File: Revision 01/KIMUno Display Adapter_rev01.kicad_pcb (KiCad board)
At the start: 2 copper layers, 50.8 x 20.1 mm, 3 parts

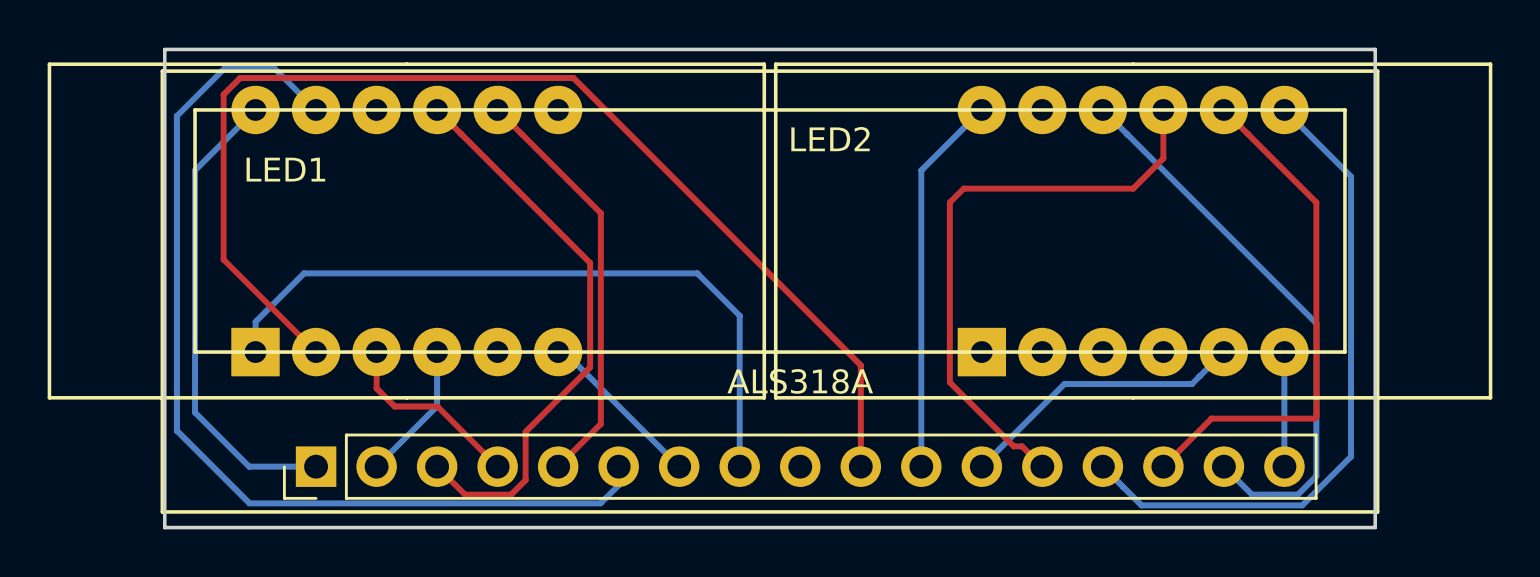
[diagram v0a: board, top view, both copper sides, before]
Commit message: Several changes
Redid the routing.
Changed the LED footprint with smaller pads.
Added logo to underside of the board.
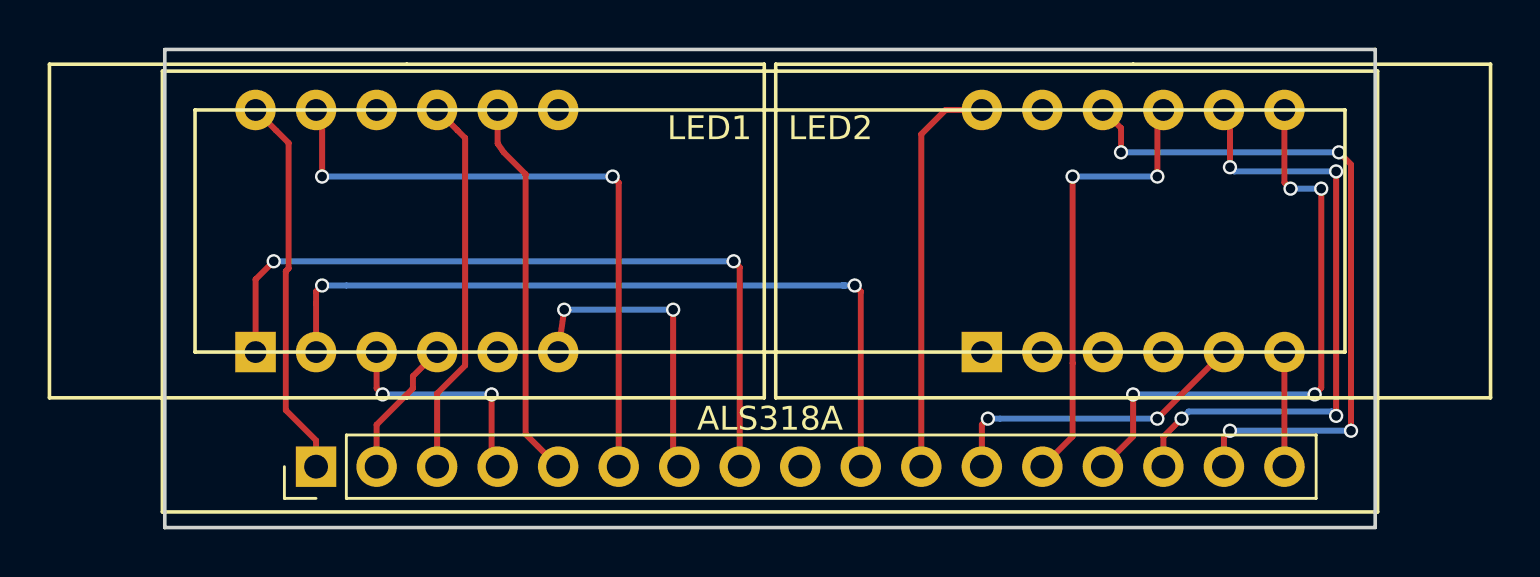
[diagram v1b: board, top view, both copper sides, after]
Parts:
- added  : , Thilo_Lib:LOGO_VintageProject_B.SilkS, F.Cu at (115.8, 69.6)
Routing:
- net /Seg_1d: track 48.7 -> 33.1 mm, vias 0 -> 2
- net /Seg_1a: track 41.5 -> 27.4 mm, vias 0 -> 2
- net /CC2: track 23.8 -> 16.3 mm
- net /CC4: track 7.07 -> 13.3 mm, vias 0 -> 2
- net /Seg_2f: track 23.8 -> 29.8 mm, vias 0 -> 4
- net /CC7: track 24.7 -> 19.2 mm, vias 0 -> 2
- net /CC8: track 21.8 -> 26.3 mm, vias 0 -> 4
- net /CC1: track 19.8 -> 16.1 mm
- net /Seg_2b: track 27.6 -> 24.6 mm, vias 1 -> 4
- net /Seg_1e: track 29.5 -> 32.2 mm, vias 0 -> 2
- net /Seg_1h: track 7.97 -> 9.59 mm, vias 0 -> 2
- net /CC3: track 17.5 -> 16.4 mm
- net /Seg_2g: track 12.2 -> 13.2 mm, vias 0 -> 2
- net /CC6: track 16.0 -> 16.9 mm
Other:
- board text added: "2018"
- board text added: "Rev. 01 / 2018-07-24"
- board text removed: "(c) 2018 VintageProject"
- board text removed: "Rev. 01 / 2018-07-23"

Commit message: Rerouted tracks - Short Board for ALS318A
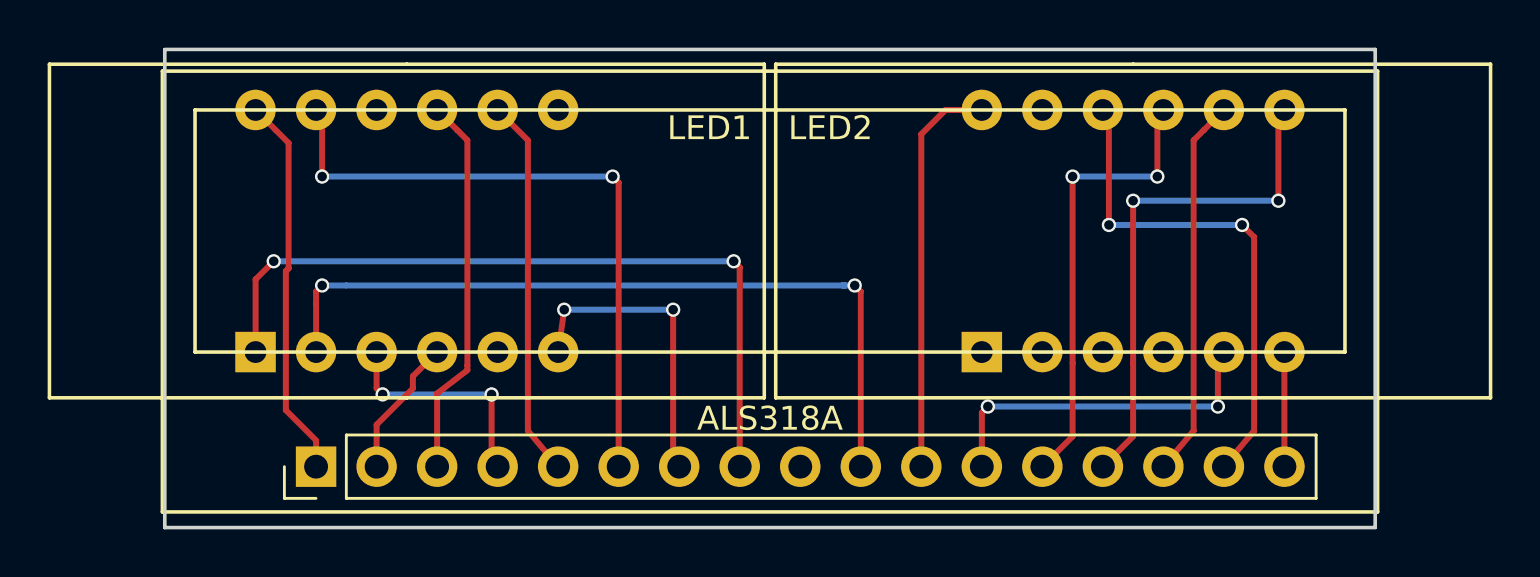
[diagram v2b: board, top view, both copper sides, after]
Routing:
- net /CC8: track 26.3 -> 16.0 mm, vias 4 -> 0
- net /Seg_2f: track 29.8 -> 21.3 mm, vias 4 -> 2
- net /Seg_2b: track 24.6 -> 21.7 mm, vias 4 -> 2
- net /Seg_2g: track 13.2 -> 14.7 mm
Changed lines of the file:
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@@
     (thickness 1.6)
     (drawings 7)
-    (tracks 120)
+    (tracks 100)
     (zones 0)
     (modules 4)
@@
   (segment (start 87.376 62.484) (end 87.63 62.23) (width 0.25) (layer F.Cu) (net 2))
   (segment (start 88.479999 63.079999) (end 87.63 62.23) (width 0.25) (layer F.Cu) (net 2))
-  (segment (start 88.805001 63.405001) (end 88.479999 63.079999) (width 0.25) (layer F.Cu) (net 2))
-  (segment (start 88.805001 72.954001) (end 88.805001 63.405001) (width 0.25) (layer F.Cu) (net 2))
-  (segment (start 87.63 74.129002) (end 88.805001 72.954001) (width 0.25) (layer F.Cu) (net 2))
+  (segment (start 88.9 63.5) (end 88.479999 63.079999) (width 0.25) (layer F.Cu) (net 2))
+  (segment (start 88.9 72.954001) (end 88.9 63.5) (width 0.25) (layer F.Cu) (net 2))
+  (segment (start 88.9 73.152) (end 88.9 72.954001) (width 0.25) (layer F.Cu) (net 2))
   (segment (start 87.63 77.2) (end 87.63 74.129002) (width 0.25) (layer F.Cu) (net 2))
-  (segment (start 90.17 63.637) (end 90.424 64.008) (width 0.25) (layer F.Cu) (net 3))
-  (segment (start 90.17 62.23) (end 90.17 63.637) (width 0.25) (layer F.Cu) (net 3))
+  (segment (start 87.63 74.129002) (end 88.9 73.152) (width 0.25) (layer F.Cu) (net 2))
   (segment (start 92.964 76.946) (end 92.71 77.2) (width 0.25) (layer F.Cu) (net 3))
-  (segment (start 91.860001 76.350001) (end 92.71 77.2) (width 0.25) (layer F.Cu) (net 3))
-  (segment (start 91.345001 75.835001) (end 91.860001 76.350001) (width 0.25) (layer F.Cu) (net 3))
-  (segment (start 91.345001 64.929001) (end 91.345001 75.835001) (width 0.25) (layer F.Cu) (net 3))
-  (segment (start 90.424 64.008) (end 91.345001 64.929001) (width 0.25) (layer F.Cu) (net 3))
+  (segment (start 91.44 63.5) (end 90.17 62.23) (width 0.25) (layer F.Cu) (net 3))
+  (segment (start 92.71 77.2) (end 91.44 75.692) (width 0.25) (layer F.Cu) (net 3))
+  (segment (start 91.44 75.692) (end 91.44 63.5) (width 0.25) (layer F.Cu) (net 3))
   (segment (start 97.52 77.2) (end 97.79 77.2) (width 0.25) (layer B.Cu) (net 4))
   (via blind (at 92.964 70.612) (size 0.6) (drill 0.4) (layers F.Cu B.Cu) (net 4))
@@
   (segment (start 117.856 62.484) (end 118.11 62.23) (width 0.25) (layer F.Cu) (net 7))
   (segment (start 117.856 65.024) (end 117.856 62.484) (width 0.25) (layer F.Cu) (net 7))
-  (via blind (at 118.872 75.184) (size 0.6) (drill 0.4) (layers F.Cu B.Cu) (net 8))
-  (segment (start 118.11 77.2) (end 118.11 75.946) (width 0.25) (layer F.Cu) (net 8))
-  (segment (start 118.11 75.946) (end 118.872 75.184) (width 0.25) (layer F.Cu) (net 8))
-  (via blind (at 125.359 75.067) (size 0.6) (drill 0.4) (layers F.Cu B.Cu) (net 8))
-  (segment (start 125.176001 74.884001) (end 125.359 75.067) (width 0.25) (layer B.Cu) (net 8))
-  (segment (start 118.872 75.184) (end 119.171999 74.884001) (width 0.25) (layer B.Cu) (net 8))
-  (segment (start 119.171999 74.884001) (end 125.176001 74.884001) (width 0.25) (layer B.Cu) (net 8))
-  (via blind (at 125.359 64.808003) (size 0.6) (drill 0.4) (layers F.Cu B.Cu) (net 8))
-  (segment (start 125.359 75.067) (end 125.359 64.808003) (width 0.25) (layer F.Cu) (net 8))
-  (via blind (at 120.904 64.633) (size 0.6) (drill 0.4) (layers F.Cu B.Cu) (net 8))
-  (segment (start 125.359 64.808003) (end 121.079003 64.808003) (width 0.25) (layer B.Cu) (net 8))
-  (segment (start 121.079003 64.808003) (end 120.904 64.633) (width 0.25) (layer B.Cu) (net 8))
-  (segment (start 120.904 62.484) (end 120.65 62.23) (width 0.25) (layer F.Cu) (net 8))
-  (segment (start 120.904 64.633) (end 120.904 62.484) (width 0.25) (layer F.Cu) (net 8))
+  (segment (start 119.38 75.692) (end 119.38 63.5) (width 0.25) (layer F.Cu) (net 8))
+  (segment (start 118.11 77.2) (end 119.38 75.692) (width 0.25) (layer F.Cu) (net 8))
+  (segment (start 119.800001 63.079999) (end 120.65 62.23) (width 0.25) (layer F.Cu) (net 8))
+  (segment (start 119.38 63.5) (end 119.800001 63.079999) (width 0.25) (layer F.Cu) (net 8))
   (segment (start 123.19 77.2) (end 123.19 72.39) (width 0.25) (layer F.Cu) (net 9))
   (segment (start 85.09 77.2) (end 85.09 75.438) (width 0.25) (layer F.Cu) (net 10))
@@
   (segment (start 100.33 68.834) (end 100.076 68.58) (width 0.25) (layer F.Cu) (net 13))
   (segment (start 100.33 77.2) (end 100.33 68.834) (width 0.25) (layer F.Cu) (net 13))
-  (via blind (at 110.744 75.184) (size 0.6) (drill 0.4) (layers F.Cu B.Cu) (net 15))
-  (via blind (at 117.856 75.184) (size 0.6) (drill 0.4) (layers F.Cu B.Cu) (net 15))
-  (segment (start 111.252 75.184) (end 117.856 75.184) (width 0.25) (layer B.Cu) (net 15))
-  (segment (start 117.856 75.184) (end 120.65 72.39) (width 0.25) (layer F.Cu) (net 15))
-  (segment (start 110.49 75.438) (end 110.744 75.184) (width 0.25) (layer F.Cu) (net 15))
-  (segment (start 110.49 77.2) (end 110.49 75.438) (width 0.25) (layer F.Cu) (net 15))
-  (segment (start 111.252 75.184) (end 110.744 75.184) (width 0.25) (layer B.Cu) (net 15))
-  (via blind (at 123.444 65.532) (size 0.6) (drill 0.4) (layers F.Cu B.Cu) (net 16))
-  (segment (start 123.19 62.23) (end 123.19 65.278) (width 0.25) (layer F.Cu) (net 16))
-  (segment (start 123.19 65.278) (end 123.444 65.532) (width 0.25) (layer F.Cu) (net 16))
-  (via blind (at 124.734 65.532) (size 0.6) (drill 0.4) (layers F.Cu B.Cu) (net 16))
-  (segment (start 123.444 65.532) (end 124.734 65.532) (width 0.25) (layer B.Cu) (net 16))
-  (via blind (at 124.46 74.168) (size 0.6) (drill 0.4) (layers F.Cu B.Cu) (net 16))
-  (segment (start 124.734 65.532) (end 124.734 73.894) (width 0.25) (layer F.Cu) (net 16))
-  (segment (start 124.734 73.894) (end 124.46 74.168) (width 0.25) (layer F.Cu) (net 16))
-  (via blind (at 116.84 74.168) (size 0.6) (drill 0.4) (layers F.Cu B.Cu) (net 16))
-  (segment (start 124.46 74.168) (end 116.84 74.168) (width 0.25) (layer B.Cu) (net 16))
-  (segment (start 116.84 75.93) (end 115.57 77.2) (width 0.25) (layer F.Cu) (net 16))
-  (segment (start 116.84 74.168) (end 116.84 75.93) (width 0.25) (layer F.Cu) (net 16))
-  (via blind (at 120.904 75.692) (size 0.6) (drill 0.4) (layers F.Cu B.Cu) (net 17))
-  (segment (start 120.65 77.2) (end 120.65 75.946) (width 0.25) (layer F.Cu) (net 17))
-  (segment (start 120.65 75.946) (end 120.904 75.692) (width 0.25) (layer F.Cu) (net 17))
-  (via blind (at 125.984 75.692) (size 0.6) (drill 0.4) (layers F.Cu B.Cu) (net 17))
-  (segment (start 120.904 75.692) (end 125.984 75.692) (width 0.25) (layer B.Cu) (net 17))
-  (via blind (at 125.476 64.008) (size 0.6) (drill 0.4) (layers F.Cu B.Cu) (net 17))
-  (segment (start 125.984 75.692) (end 125.984 64.516) (width 0.25) (layer F.Cu) (net 17))
-  (segment (start 125.984 64.516) (end 125.476 64.008) (width 0.25) (layer F.Cu) (net 17))
-  (via blind (at 116.332 64.008) (size 0.6) (drill 0.4) (layers F.Cu B.Cu) (net 17))
-  (segment (start 125.476 64.008) (end 116.332 64.008) (width 0.25) (layer B.Cu) (net 17))
-  (segment (start 116.332 62.992) (end 115.57 62.23) (width 0.25) (layer F.Cu) (net 17))
-  (segment (start 116.332 64.008) (end 116.332 62.992) (width 0.25) (layer F.Cu) (net 17))
+  (via blind (at 110.744 74.676) (size 0.6) (drill 0.4) (layers F.Cu B.Cu) (net 15))
+  (segment (start 110.49 77.2) (end 110.49 74.93) (width 0.25) (layer F.Cu) (net 15))
+  (segment (start 110.49 74.93) (end 110.744 74.676) (width 0.25) (layer F.Cu) (net 15))
+  (via blind (at 120.396 74.676) (size 0.6) (drill 0.4) (layers F.Cu B.Cu) (net 15))
+  (segment (start 110.744 74.676) (end 120.396 74.676) (width 0.25) (layer B.Cu) (net 15))
+  (segment (start 120.396 72.644) (end 120.65 72.39) (width 0.25) (layer F.Cu) (net 15))
+  (segment (start 120.396 74.676) (end 120.396 72.644) (width 0.25) (layer F.Cu) (net 15))
+  (via blind (at 116.84 66.04) (size 0.6) (drill 0.4) (layers F.Cu B.Cu) (net 16))
+  (segment (start 116.84 72.859002) (end 116.84 66.04) (width 0.25) (layer F.Cu) (net 16))
+  (segment (start 115.57 77.2) (end 116.84 75.93) (width 0.25) (layer F.Cu) (net 16))
+  (segment (start 116.84 75.93) (end 116.84 72.859002) (width 0.25) (layer F.Cu) (net 16))
+  (via blind (at 122.936 66.04) (size 0.6) (drill 0.4) (layers F.Cu B.Cu) (net 16))
+  (segment (start 116.84 66.04) (end 122.936 66.04) (width 0.25) (layer B.Cu) (net 16))
+  (segment (start 122.936 62.484) (end 123.19 62.23) (width 0.25) (layer F.Cu) (net 16))
+  (segment (start 122.936 66.04) (end 122.936 62.484) (width 0.25) (layer F.Cu) (net 16))
+  (via blind (at 121.412 67.056) (size 0.6) (drill 0.4) (layers F.Cu B.Cu) (net 17))
+  (via blind (at 115.824 67.056) (size 0.6) (drill 0.4) (layers F.Cu B.Cu) (net 17))
+  (segment (start 121.412 67.056) (end 115.824 67.056) (width 0.25) (layer B.Cu) (net 17))
+  (segment (start 115.824 62.484) (end 115.57 62.23) (width 0.25) (layer F.Cu) (net 17))
+  (segment (start 115.824 67.056) (end 115.824 62.484) (width 0.25) (layer F.Cu) (net 17))
+  (segment (start 121.92 67.564) (end 121.412 67.056) (width 0.25) (layer F.Cu) (net 17))
+  (segment (start 121.92 75.692) (end 121.92 67.564) (width 0.25) (layer F.Cu) (net 17))
+  (segment (start 120.65 77.2) (end 121.92 75.692) (width 0.25) (layer F.Cu) (net 17))
   (via blind (at 105.156 69.596) (size 0.6) (drill 0.4) (layers F.Cu B.Cu) (net 18))
   (segment (start 105.156 69.596) (end 104.648 69.596) (width 0.25) (layer B.Cu) (net 18))
